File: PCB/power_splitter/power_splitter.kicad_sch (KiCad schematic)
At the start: 30 parts, among them Q2 IRLZ44N, U1 AP62300TWU, U2 AP62300TWU

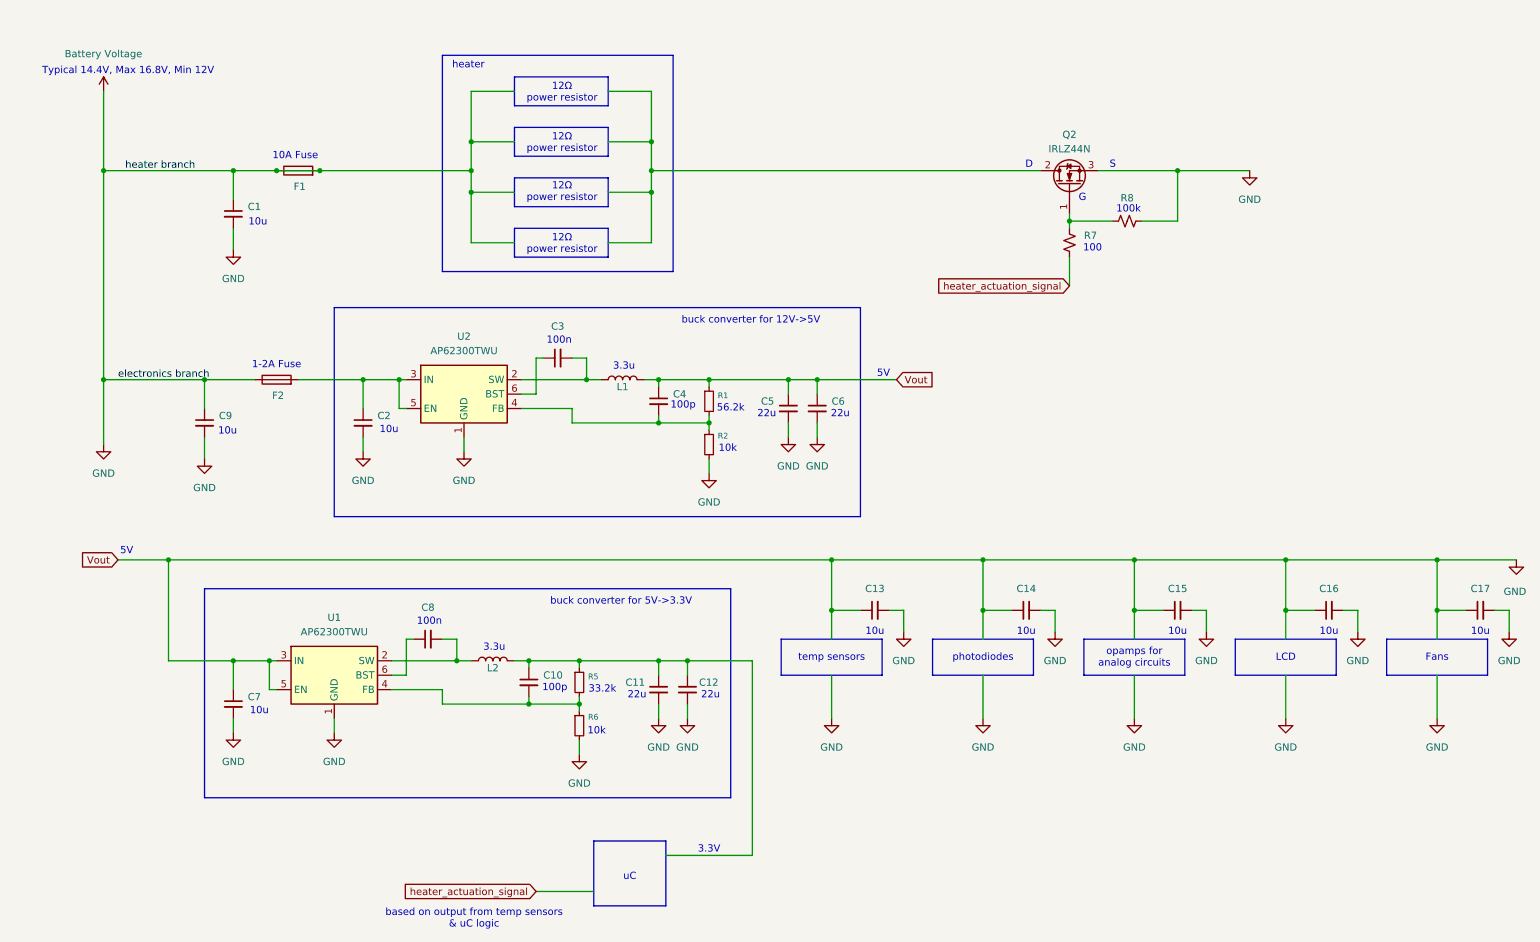
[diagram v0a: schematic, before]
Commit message: updated power circuit
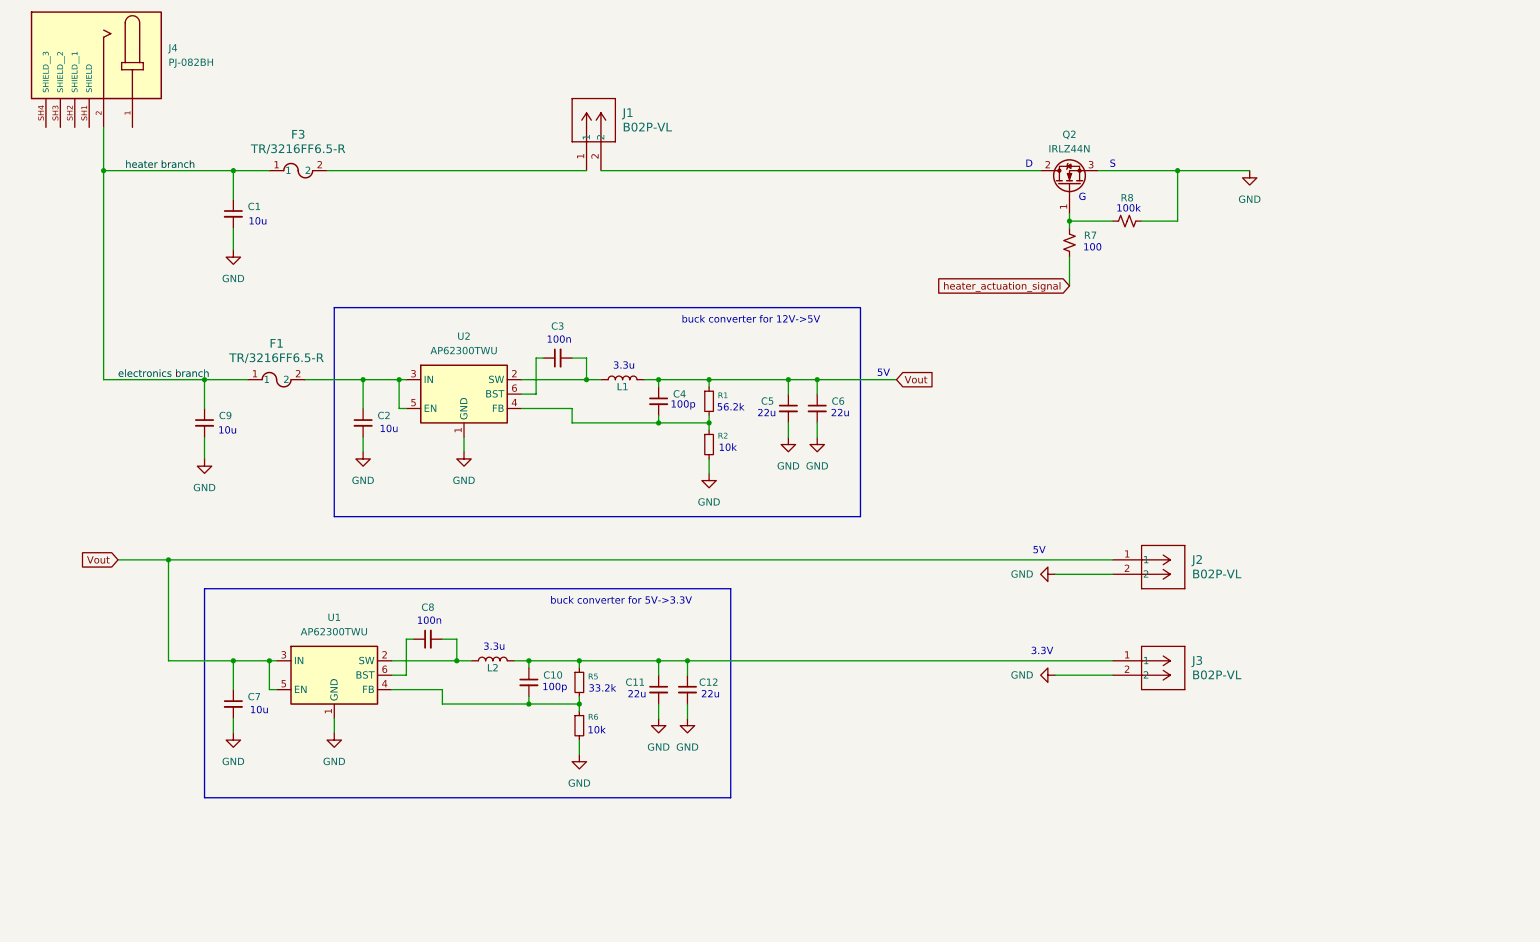
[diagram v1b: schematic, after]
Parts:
- removed C13, C14, C15, C16, C17: C_Small, symbol Device:C_Small
- removed F1, F2: Fuse, symbol Device:Fuse
- added F1, F3: TR/3216FF6.5-R, FUSE:FUS_CB_3216FF, symbol 2026-01-28_20-55-13:TR_3216FF6.5-R
- added J1, J2, J3: B02P-VL, Connector_JST:JST_NV_B02P-NV_1x02_P5.00mm_Vertical, symbol B02P_VL_2026-01-28_20-34-11:B02P_VL_CONNECTOR
- added J4: PJ-082BH, PJ_082BH:SAMESKY_PJ-082BH, symbol PJ-082BH:PJ-082BH
- C1, C10, C11, C12, C2, C3, C4, C5, C6, C7, C8, C9: footprint (none) -> Capacitor_SMD:C_1206_3216Metric
- L1, L2: footprint (none) -> Inductor_THT:L_Axial_L7.0mm_D3.3mm_P5.08mm_Vertical_Fastron_MICC
- R1, R2, R5, R6, R7, R8: footprint (none) -> RESISTOR:YAG_MF25_YAG
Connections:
- net at Q2.2 (D): now also J1.2
- net at C2.1, U2.3 (IN), U2.5 (EN): now also F1.2
- net at C10.1, C11.1, C12.1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: now also J3.1
- net Battery Voltage renamed GND
- net GND: now also J2.2, J3.2; no longer C1.1, C4.1, C5.1, C6.1, C7.1, C9.1, L1.2, R1.1, U1.3 (IN), U1.5 (EN)
- new net: F3.2, J1.1
- new net Vout: C4.1, C5.1, C6.1, C7.1, J2.1, L1.2, R1.1, U1.3 (IN), U1.5 (EN)
- new net electronics branch: C1.1, C9.1, F1.1, F3.1, J4.2
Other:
- note removed: "1-2A Fuse"
- note removed: "10A Fuse"
- note removed: "12Ω power resistor"
- note removed: "Fans"
- note removed: "LCD"
- note removed: "Typical 14.4V, Max 16.8V, Min 12V"
- note removed: "based on output from temp sensors & uC logic"
- note removed: "heater"
- note removed: "opamps for analog circuits"
- note removed: "photodiodes"
- note removed: "temp sensors"
- note removed: "uC"

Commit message: power stuff
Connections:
- net GND: now also J4.SH1 (SHIELD), J4.SH2 (SHIELD__1), J4.SH3 (SHIELD__2), J4.SH4 (SHIELD__3)
- net 3V_Line: now reaches C10.1, C11.1, C12.1, J3.1, L2.2, R5.1
- net Vout renamed 5V_Line

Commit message: Liv's stuff
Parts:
- added J5: B02P-VL, Connector_JST:JST_NV_B02P-NV_1x02_P5.00mm_Vertical, symbol B02P_VL_2026-01-28_20-34-11:B02P_VL_CONNECTOR
- C1, C10, C11, C12, C2, C3, C4, C5, C6, C7, C8, C9: footprint Capacitor_SMD:C_1206_3216Metric -> Capacitor_SMD:C_1206_3216Metric_Pad1.33x1.80mm_HandSolder
- J1, J2, J3: footprint Connector_JST:JST_NV_B02P-NV_1x02_P5.00mm_Vertical -> B02P_new:CONN_B02P-VL_JST
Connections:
- net GND: now also J4.1, J5.2
- net heater_actuation_signal: now also J5.1

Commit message: Liv's stuff
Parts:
- added Thermal_Fuse_1, Thermal_Fuse_2: R_Small, RESISTOR:YAG_MF25_YAG, symbol Device:R_Small
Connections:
- net at J1.1: now also Thermal_Fuse_1.2; no longer F3.2
- net at C2.1, U2.3 (IN), U2.5 (EN): now also Thermal_Fuse_2.2; no longer F1.2
- new net: F3.2, Thermal_Fuse_1.1
- new net: F1.2, Thermal_Fuse_2.1
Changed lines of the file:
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@@
 	(wire
 		(pts
-			(xy 63.5 81.28) (xy 73.66 81.28)
+			(xy 63.5 81.28) (xy 66.04 81.28)
 		)
 		(stroke
@@
 	(wire
 		(pts
-			(xy 67.31 44.45) (xy 113.03 44.45)
+			(xy 67.31 44.45) (xy 77.47 44.45)
 		)
 		(stroke
@@
 	(wire
 		(pts
+			(xy 71.12 81.28) (xy 73.66 81.28)
+		)
+		(stroke
+			(width 0)
+			(type default)
+		)
+	)
+	(wire
+		(pts
 			(xy 81.28 133.35) (xy 81.28 127)
 		)
@@
 		(pts
 			(xy 87.63 127) (xy 90.17 127)
+		)
+		(stroke
+			(width 0)
+			(type default)
+		)
+	)
+	(wire
+		(pts
+			(xy 82.55 44.45) (xy 113.03 44.45)
 		)
 		(stroke
@@
 	)
 	(symbol
+		(lib_id "Device:R_Small")
+		(at 80.01 44.45 90)
+		(unit 1)
+		(exclude_from_sim no)
+		(in_bom yes)
+		(on_board yes)
+		(dnp no)
+		(property "Reference" "Thermal_Fuse_1"
+			(at 78.994 42.926 0)
+			(effects
+				(font
+					(size 1.016 1.016)
+				)
+				(justify left)
+			)
+		)
+		(property "Value" "R_Small"
+			(at 81.2799 41.91 0)
+			(effects
+				(font
+					(size 1.27 1.27)
+				)
+				(justify left)
+				(hide yes)
+			)
+		)
+		(property "Footprint" "RESISTOR:YAG_MF25_YAG"
+			(at 80.01 44.45 0)
+			(effects
+				(font
+					(size 1.27 1.27)
+				)
+				(hide yes)
+			)
+		)
+		(property "Datasheet" "~"
+			(at 80.01 44.45 0)
+			(effects
+				(font
+					(size 1.27 1.27)
+				)
+				(hide yes)
+			)
+		)
+		(property "Description" "Resistor, small symbol"
+			(at 80.01 44.45 0)
+			(effects
+				(font
+					(size 1.27 1.27)
+				)
+				(hide yes)
+			)
+		)
+		(pin "1"
+		)
+		(pin "2"
+		)
+		(instances
+			(project "power_splitter"
+				(path "/4cdb7044-92dd-4272-b0bd-7079be4f3079"
+					(reference "Thermal_Fuse_1")
+					(unit 1)
+				)
+			)
+		)
+	)
+	(symbol
 		(lib_id "power:GND")
 		(at 148.59 91.44 0)
@@
 					(unit 1)
 				)
+			)
+		)
+	)
+	(symbol
+		(lib_id "Device:R_Small")
+		(at 68.58 81.28 90)
+		(unit 1)
+		(exclude_from_sim no)
+		(in_bom yes)
+		(on_board yes)
+		(dnp no)
+		(property "Reference" "Thermal_Fuse_2"
+			(at 67.564 79.756 0)
+			(effects
+				(font
+					(size 1.016 1.016)
+				)
+				(justify left)
+			)
+		)
+		(property "Value" "R_Small"
+			(at 69.8499 78.74 0)
+			(effects
+				(font
+					(size 1.27 1.27)
+				)
+				(justify left)
+				(hide yes)
+			)
+		)
+		(property "Footprint" "RESISTOR:YAG_MF25_YAG"
+			(at 68.58 81.28 0)
+			(effects
+				(font
+					(size 1.27 1.27)
+				)
+				(hide yes)
+			)
+		)
+		(property "Datasheet" "~"
+			(at 68.58 81.28 0)
+			(effects
+				(font
+					(size 1.27 1.27)
+				)
+				(hide yes)
+			)
+		)
+		(property "Description" "Resistor, small symbol"
+			(at 68.58 81.28 0)
+			(effects
+				(font
+					(size 1.27 1.27)
+				)
+				(hide yes)
+			)
+		)
+		(pin "1"
+		)
+		(pin "2"
+		)
+		(instances
+			(project "power_splitter"
+				(path "/4cdb7044-92dd-4272-b0bd-7079be4f3079"
+					(reference "Thermal_Fuse_2")
+					(unit 1)
+				)
